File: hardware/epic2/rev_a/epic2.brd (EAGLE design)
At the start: 23.5 x 17 mm, 32 parts, among them J1 PINHD-1X10/0.050, J2 PINHD-1X10/0.050, J3 PINHD-1X10/0.050, U2 FM25LBTDFN-8, U3 CC2538, X1 EPSON-FA-128, X2 FC-12M32.7680KA-A3

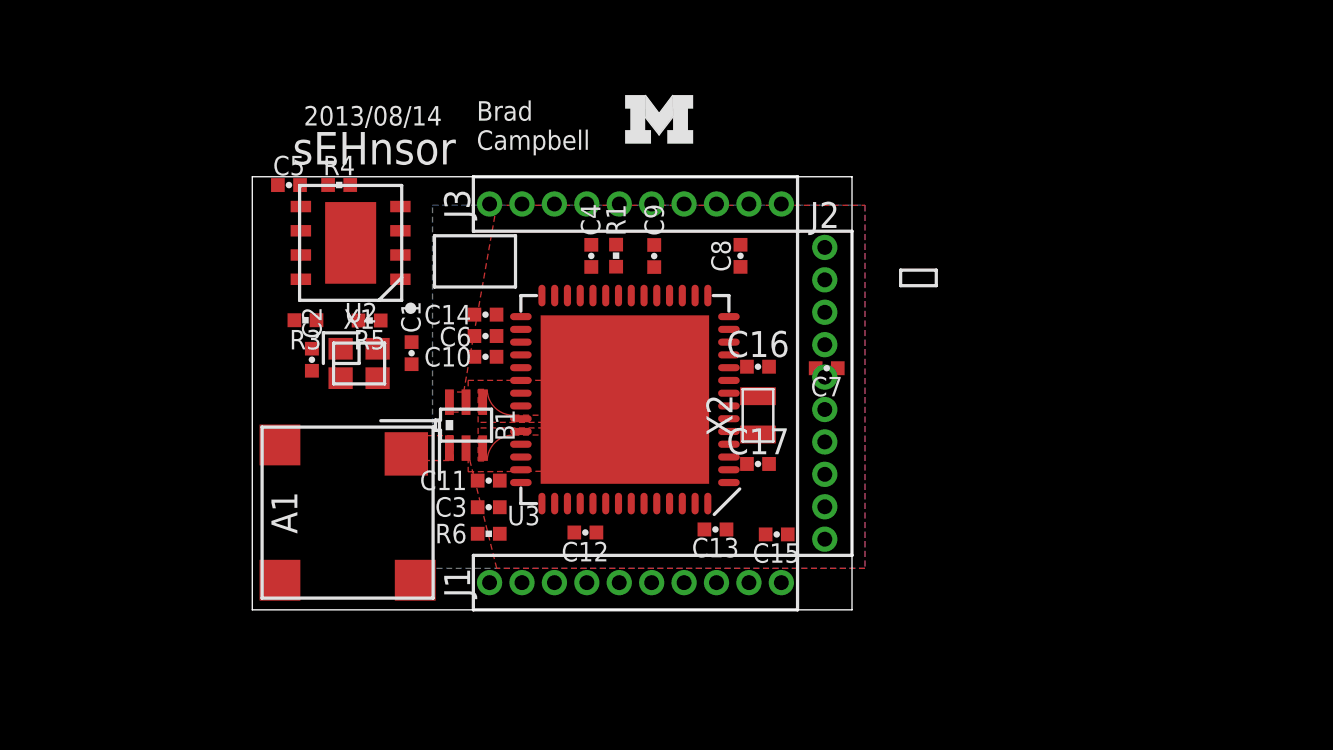
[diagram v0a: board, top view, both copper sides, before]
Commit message: new headers
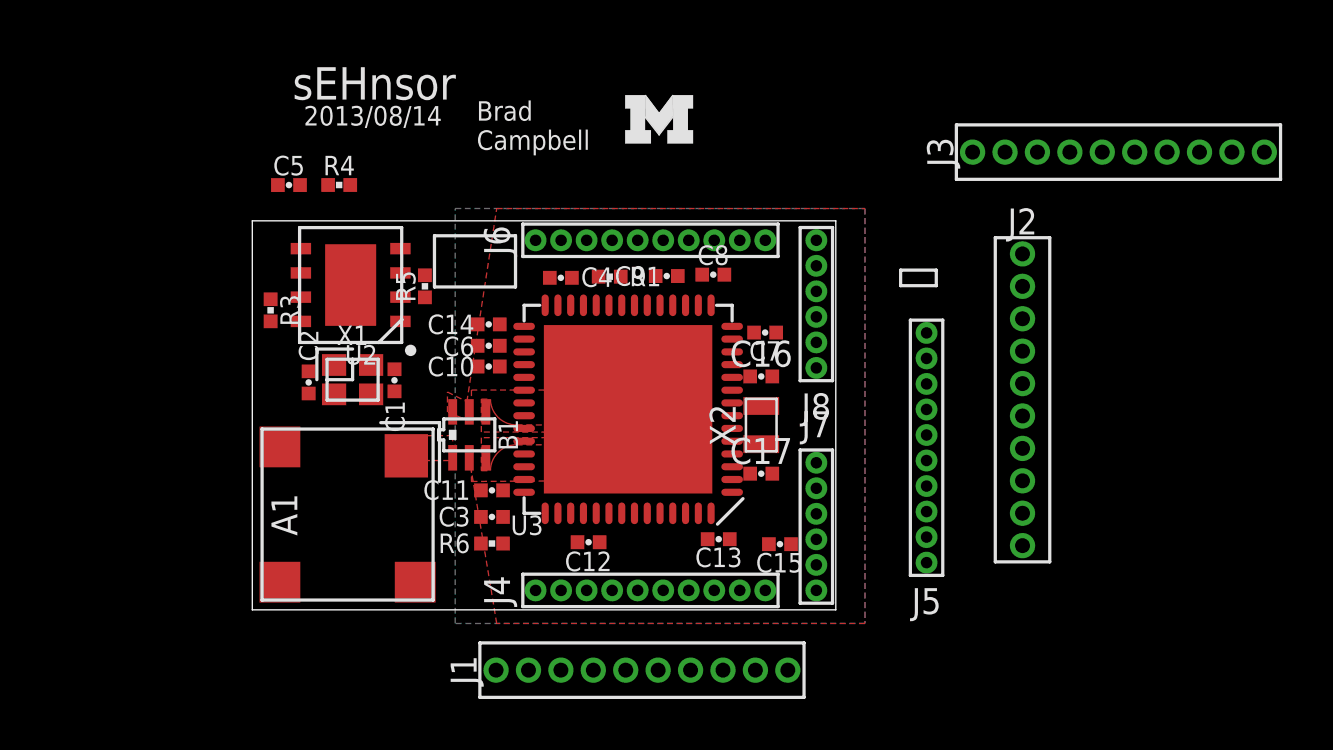
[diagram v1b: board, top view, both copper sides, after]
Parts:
- added J4, J5, J6: PINHD-1X10/1MM, headers:1X10/1MM
- added J7, J8: PINHD-1X06/1MM, headers:1X6/1MM
- moved J3 19.0 mm to (33.9, 17.9)
- moved J2 7.75 mm to (30.2, 8.23)
- moved J1 3.44 mm to (15.3, -2.36)
- moved C7 2.79 mm to (20.1, 10.9)
- moved R5 2.55 mm to (6.76, 12.7), turned to 270 degrees
- moved U2 1.65 mm to (3.85, 12.7)
- moved C4 1.47 mm to (12.1, 13.0), turned to 0 degrees
- moved R3 1.42 mm to (0.72, 11.7), turned to 270 degrees
- moved C8 1.30 mm to (18.1, 13.1), turned to 0 degrees
- moved C1 1.26 mm to (5.57, 8.99), turned to 270 degrees
- moved C9 0.93 mm to (16.2, 13.1), turned to 180 degrees
- moved C2 0.90 mm to (2.21, 8.91)
- moved R1 0.86 mm to (14.0, 13.1), turned to 180 degrees
- moved X1 0.68 mm to (3.93, 9.02)
- moved C10 0.40 mm to (9.26, 9.53)
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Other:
- board size 23.5 x 17 mm -> 22.9 x 15.2 mm

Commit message: dummy routing for epic2
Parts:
- removed J1, J2, J3: PINHD-1X10/0.050, headers:1X10-0.050
- removed J5: PINHD-1X10/1MM, headers:1X10/1MM
- removed R5: 4.7k, passives:0402_RES
- added C18: 10nF, passives:0402_CAP
- added D1: SML-LX0404SIUPGUSB, leds:1MM_SQ_4PAD
- added R2: 1k, passives:0402_RES
- added U1: RV-4162-C7, chips:MICRO-CRYSTAL-C7
- R3, R4: value 4.7k -> 1k
- moved U$1 20.4 mm to (-3.05, 7.98)
- moved R3 19.9 mm to (20.2, 8.13), turned to 180 degrees
- moved R4 19.3 mm to (20.2, 7.24), turned to 180 degrees
- moved C16 11.5 mm to (10.7, 2.29), turned to 270 degrees
- moved X2 9.09 mm to (12.3, 2.29), turned to 0 degrees
- moved C17 6.70 mm to (14.0, 2.29), turned to 270 degrees
- moved C5 5.14 mm to (5.72, 13.8), turned to 270 degrees
- moved C12 3.90 mm to (9.37, 1.80), turned to 180 degrees
- moved R1 3.69 mm to (10.3, 13.0), turned to 270 degrees
- moved C9 2.53 mm to (13.7, 13.1), turned to 0 degrees
- moved C15 1.52 mm to (19.2, 2.83)
- moved U2 1.23 mm to (2.62, 12.8), turned to 270 degrees
- moved C13 1.15 mm to (19.2, 2.06), turned to 0 degrees
- moved C8 1.05 mm to (19.0, 12.7)
- moved C2 1.02 mm to (3.23, 9.04)
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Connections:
- removed net A3: U3.19
- removed net A4: U3.20
- removed net A5: U3.21
- removed net A6: U3.22
- removed net A7: U3.23
- removed net DS2411: U3.5
- removed net MISO: U2.2
- removed net MOSI: U2.5
- removed net SCK: U2.6
- new net !RTC_INT: U1.6, U3.49
- new net ADC3: J6.4, U3.19
- new net ADC4: J6.5, U3.20
- new net ADC5: J6.6, U3.21
- new net ADC6: J6.7, U3.22
- new net ADC7: J6.8, U3.23
- new net B1: J4.10, U3.54
- new net B2: J4.9, U3.53
- new net B3: J4.8, U3.52
- new net B4: J4.7, U3.51
- new net DGND_USB: J7.1, U3.1
- new net DVDD_USB: J7.4, U3.4
- new net I2C_SCL: J8.2, U1.8, U3.8
- new net I2C_SDA: J8.3, U1.1, U3.9
- new net LED_BLUE: R4.2, U3.6
- new net LED_GREEN: R3.2, U3.7
- new net LED_RED: R2.2, U3.5
- new net N$11: D1.4, R3.1
- new net N$12: D1.3, R4.1
- new net N$7: D1.2, R2.1
- new net RTC_CLKOUT: U1.2, U3.50
- new net SPI_MISO: J7.5, U2.2, U3.25
- new net SPI_MOSI: J7.6, U2.5, U3.26
- new net SPI_SCK: J8.1, U2.6, U3.27
- new net UNUSED1: J4.2
- new net UNUSED2: J4.3
- new net USB_N: J7.3, U3.3
- new net USB_P: J7.2, U3.2
- net !FRAM_CS: now also U3.30; no longer R3.1, U3.51
- net !FRAM_HOLD: now also U3.29; no longer R4.1, U3.52
- net !FRAM_WP: now also U3.31; no longer R5.1, U3.50
- net !RESET: now also J6.9
- net BOOTLOADER_CTRL: now also J6.3
- net BOOTLOADER_RX: now also J6.1
- net BOOTLOADER_TX: now also J6.2
- net C0: now also J8.6
- net C1: now also J8.5
- net C2: now also J8.4
- net GND: now also C18.2, J6.10, U1.3
- net TCK: now also J4.5
- net TDO: now also J4.6
- net TMS: now also J4.4
- net VCC: now also C18.1, D1.1, J4.1, U1.5; no longer R3.2, R4.2, R5.2
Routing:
- net RTC_CLKOUT: track 0.00 -> 26.2 mm, vias 0 -> 2
- net !RTC_INT: track 0.00 -> 23.8 mm, vias 0 -> 2
- net VCC: track 0.00 -> 22.0 mm
- net I2C_SDA: track 0.00 -> 22.0 mm, vias 0 -> 1
- net I2C_SCL: track 0.00 -> 20.3 mm, vias 0 -> 1
- net SPI_MISO: track 0.00 -> 14.7 mm, vias 0 -> 2
- net !FRAM_CS: track 0.00 -> 13.3 mm, vias 0 -> 2
- net !FRAM_WP: track 0.00 -> 11.5 mm, vias 0 -> 2
- net SPI_MOSI: track 0.00 -> 11.0 mm, vias 0 -> 2
- net N$10: track 0.00 -> 9.73 mm, vias 0 -> 2
- net SPI_SCK: track 0.00 -> 7.80 mm, vias 0 -> 2
- net !FRAM_HOLD: track 0.00 -> 6.97 mm, vias 0 -> 2
- net N$9: track 0.00 -> 5.44 mm, vias 0 -> 2
- net DGND_USB: track 0.00 -> 5.21 mm
- net B1: track 0.00 -> 4.93 mm
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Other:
- board text added: "BC"
- board text removed: "Brad Campbell"

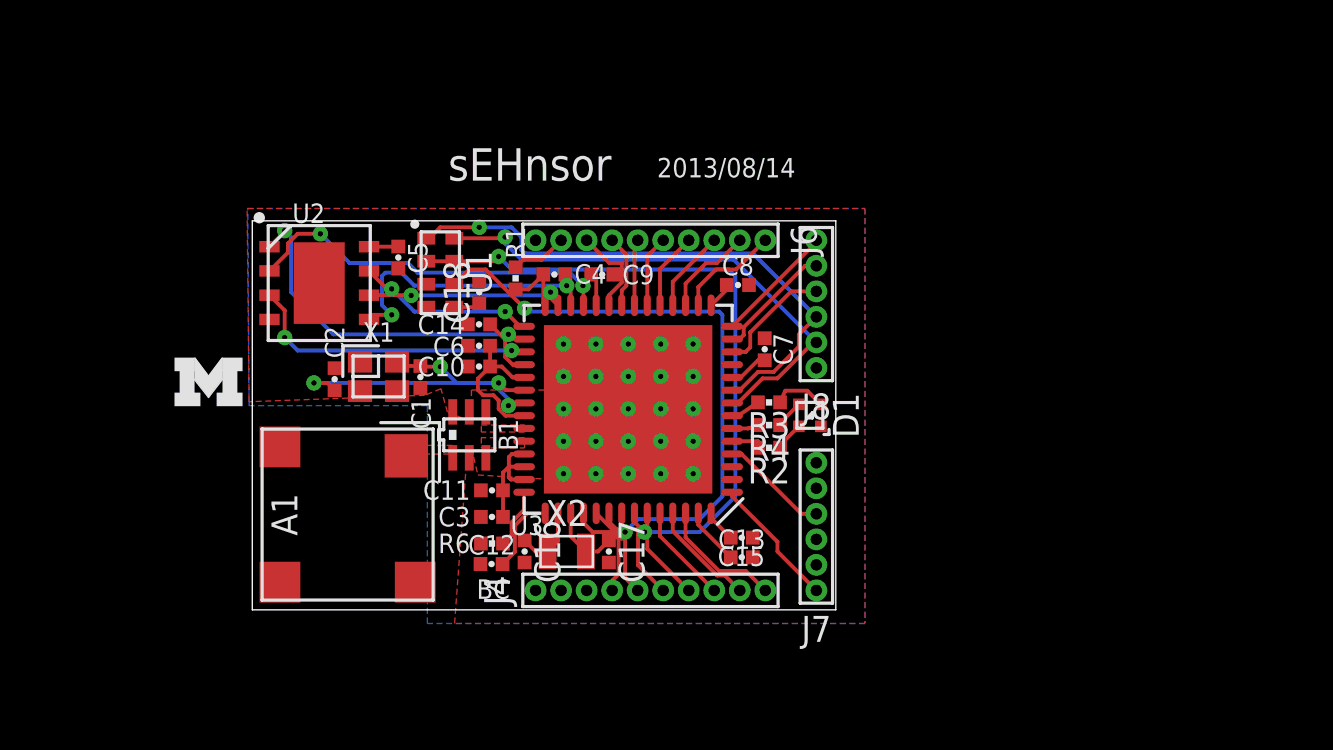
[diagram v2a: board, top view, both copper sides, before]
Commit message: rectangular board close to routed
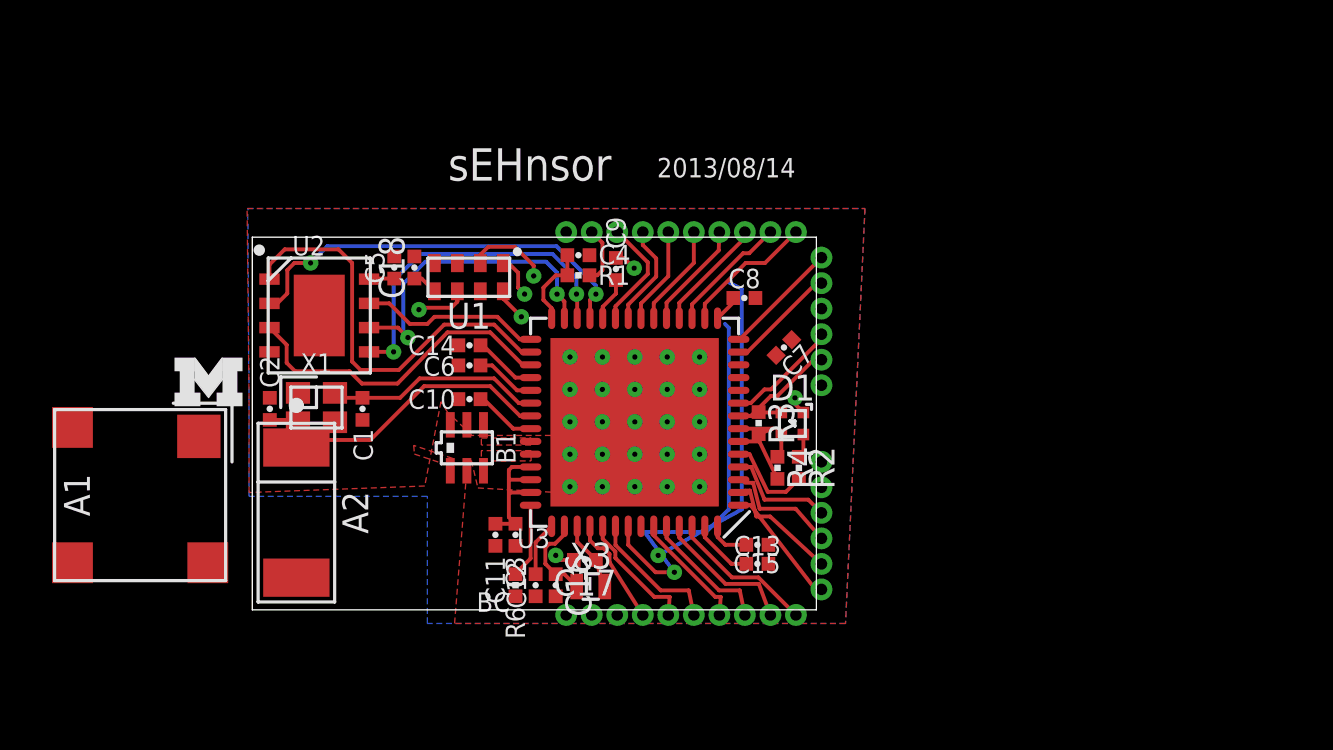
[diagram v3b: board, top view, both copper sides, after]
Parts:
- removed J4, J6: PINHD-1X10/1MM, headers:1X10/1MM
- removed J7, J8: PINHD-1X06/1MM, headers:1X6/1MM
- removed X2: FC-12M32.7680KA-A3, crystals:FC-12M
- added A2: FRACTUS-2.4GHZ-FR05-S1-N-0-102, chips:FRACTUS-ANTENNA-FR05-S1-N-0-102
- added U$2: EPIC2-HEADER, epic2:EPIC2-HEADER
- added X3: ABS05-32.768KHZ-T, crystals:ABS05
- moved A1 8.16 mm to (-4.39, 4.50)
- moved C2 2.79 mm to (0.69, 7.87)
- moved X1 2.72 mm to (2.51, 7.92)
- moved C18 2.72 mm to (6.35, 13.4)
- moved C1 2.59 mm to (4.32, 7.87)
- moved R1 2.46 mm to (12.8, 13.1), turned to 180 degrees
- moved C12 1.92 mm to (11.1, 0.97), turned to 270 degrees
- moved R6 1.88 mm to (10.3, 0.97), turned to 270 degrees
- moved C16 1.80 mm to (11.9, 0.97)
- moved C11 1.75 mm to (9.53, 2.94), turned to 270 degrees
- moved R4 1.71 mm to (20.6, 5.56), turned to 270 degrees
- moved R2 1.41 mm to (21.4, 5.56), turned to 270 degrees
- moved C10 1.33 mm to (8.51, 8.26)
- moved U2 1.27 mm to (2.62, 11.5)
- moved C4 1.21 mm to (12.8, 13.9)
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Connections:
- net !RESET: now also U$2.31; no longer J6.9
- net ADC3: now also U$2.26; no longer J6.4
- net ADC4: now also U$2.27; no longer J6.5
- net ADC5: now also U$2.28; no longer J6.6
- net ADC6: now also U$2.29; no longer J6.7
- net ADC7: now also U$2.30; no longer J6.8
- net B1: now also U$2.10; no longer J4.10
- net B2: now also U$2.9; no longer J4.9
- net B3: now also U$2.8; no longer J4.8
- net B4: now also U$2.7; no longer J4.7
- net BOOTLOADER_CTRL: now also U$2.25; no longer J6.3
- net BOOTLOADER_RX: now also U$2.23; no longer J6.1
- net BOOTLOADER_TX: now also U$2.24; no longer J6.2
- net C0: now also U$2.22; no longer J8.6
- net C1: now also U$2.21; no longer J8.5
- net C2: now also U$2.20; no longer J8.4
- net DGND_USB: now also U$2.11; no longer J7.1
- net DVDD_USB: now also U$2.14; no longer J7.4
- net GND: now also U$2.32; no longer J6.10
- net I2C_SCL: now also U$2.18; no longer J8.2
- net I2C_SDA: now also U$2.19; no longer J8.3
- net N$13: now also X3.B; no longer X2.2
- net N$6: now also X3.A; no longer X2.1
- net SPI_MISO: now also U$2.15; no longer J7.5
- net SPI_MOSI: now also U$2.16; no longer J7.6
- net SPI_SCK: now also U$2.17; no longer J8.1
- net TCK: now also U$2.5; no longer J4.5
- net TDO: now also U$2.6; no longer J4.6
- net TMS: now also U$2.4; no longer J4.4
- net UNUSED1: now also U$2.2; no longer J4.2
- net UNUSED2: now also U$2.3; no longer J4.3
- net USB_N: now also U$2.13; no longer J7.3
- net USB_P: now also U$2.12; no longer J7.2
- net VCC: now also U$2.1; no longer J4.1
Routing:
- net I2C_SDA: track 22.0 -> 6.15 mm
- net I2C_SCL: track 20.3 -> 5.45 mm
- net RTC_CLKOUT: track 26.2 -> 16.5 mm
- net !RTC_INT: track 23.8 -> 18.4 mm
- net SPI_SCK: track 7.80 -> 12.7 mm
- net C2: track 4.62 -> 0.00 mm
- net USB_P: track 0.00 -> 4.51 mm
- net USB_N: track 0.00 -> 4.32 mm
- net !FRAM_CS: track 13.3 -> 16.4 mm, vias 2 -> 0
- net N$9: track 5.44 -> 8.50 mm, vias 2 -> 0
- net SPI_MOSI: track 11.0 -> 13.3 mm
- net LED_RED: track 1.27 -> 3.49 mm
- net N$10: track 9.73 -> 11.9 mm, vias 2 -> 0
- net GND: track 0.00 -> 1.66 mm, vias 9 -> 27
- net SPI_MISO: track 14.7 -> 16.3 mm
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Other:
- board size 22.9 x 15.2 mm -> 22.1 x 14.6 mm

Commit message: workin on epic2
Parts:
- removed U$2: EPIC2-HEADER, epic2:EPIC2-HEADER
- added J1: EPIC2-HEADER2, epic2:EPIC2-HEADER2
- moved R2 26.5 mm to (-2.46, 17.0)
- moved R4 25.1 mm to (-1.78, 17.0)
- moved R3 23.0 mm to (-0.99, 17.0)
- moved D1 22.4 mm to (0.95, 17.0), turned to 90 degrees
- moved U2 4.83 mm to (5.42, 15.5)
- moved X3 4.29 mm to (8.97, 0.89)
- moved C12 4.17 mm to (6.93, 1.09)
- moved C16 4.17 mm to (7.72, 1.09)
- moved R6 4.17 mm to (6.15, 1.09)
- moved U1 4.12 mm to (11.8, 15.4)
- moved C18 4.09 mm to (9.47, 16.1)
- moved C1 4.09 mm to (3.40, 11.9)
- moved C8 4.09 mm to (15.2, 12.7), turned to 90 degrees
- moved X1 4.01 mm to (1.73, 11.9)
- moved C5 3.72 mm to (8.18, 16.1)
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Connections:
- removed net B1: U$2.10, U3.54
- removed net B2: U$2.9, U3.53
- removed net UNUSED2: U$2.3
- new net B5: J1.7, U3.50
- new net B6: J1.6, U3.49
- net !RESET: now also J1.31; no longer U$2.31
- net !RTC_INT: now also U3.54; no longer U3.49
- net ADC3: now also J1.26; no longer U$2.26
- net ADC4: now also J1.27; no longer U$2.27
- net ADC5: now also J1.28; no longer U$2.28
- net ADC6: now also J1.29; no longer U$2.29
- net ADC7: now also J1.30; no longer U$2.30
- net B3: now also J1.9; no longer U$2.8
- net B4: now also J1.8; no longer U$2.7
- net BOOTLOADER_CTRL: now also J1.25; no longer U$2.25
- net BOOTLOADER_RX: now also J1.23; no longer U$2.23
- net BOOTLOADER_TX: now also J1.24; no longer U$2.24
- net C0: now also J1.22; no longer U$2.22
- net C1: now also J1.21; no longer U$2.21
- net C2: now also J1.20; no longer U$2.20
- net C3: now also J1.19
- net DGND_USB: now also J1.10; no longer U$2.11
- net DVDD_USB: now also J1.13; no longer U$2.14
- net GND: now also J1.32; no longer U$2.32
- net I2C_SCL: now also J1.17; no longer U$2.18
- net I2C_SDA: now also J1.18; no longer U$2.19
- net LED_BLUE: no longer U3.6
- net LED_GREEN: no longer U3.7
- net LED_RED: no longer U3.5
- net RTC_CLKOUT: now also U3.53; no longer U3.50
- net SPI_MISO: now also J1.14, U3.5; no longer U$2.15
- net SPI_MOSI: now also J1.15, U3.6; no longer U$2.16
- net SPI_SCK: now also J1.16, U3.7; no longer U$2.17
- net TCK: now also J1.4; no longer U$2.5
- net TDO: now also J1.5; no longer U$2.6
- net TMS: now also J1.3; no longer U$2.4
- net UNUSED1: now also J1.2; no longer U$2.2
- net USB_N: now also J1.12; no longer U$2.13
- net USB_P: now also J1.11; no longer U$2.12
- net VCC: now also J1.1; no longer U$2.1
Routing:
- net !FRAM_WP: track 12.9 -> 3.86 mm
- net !RTC_INT: track 18.4 -> 9.61 mm, vias 2 -> 1
- net N$10: track 11.9 -> 4.70 mm
- net B1: track 5.76 -> 0.00 mm
- net B2: track 5.61 -> 0.00 mm
- net BOOTLOADER_RX: track 5.30 -> 0.00 mm
- net !FRAM_CS: track 16.4 -> 11.2 mm
- net BOOTLOADER_TX: track 4.79 -> 0.00 mm
- net C0: track 4.57 -> 0.04 mm
- net VCC: track 20.5 -> 16.0 mm, vias 1 -> 0
- net BOOTLOADER_CTRL: track 4.45 -> 0.00 mm
- net ADC3: track 4.22 -> 0.00 mm
- net ADC4: track 4.03 -> 0.00 mm
- net C1: track 4.36 -> 0.34 mm
- net B5: track 0.00 -> 3.92 mm
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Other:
- board size 22.1 x 14.6 mm -> 18 x 18 mm
- board text removed: "2013/08/14"
- board text removed: "sEHnsor"

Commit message: getting closer with epic2
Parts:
- removed A1: FRACTUS-2.4GHZ-FR05-S1-N-0-001, chips:FRACTUS-ANTENNA-FR05-S1-N-0-001
- removed C7: 0.1uF, passives:0402_CAP
- added C20: 0.1uF, rcl:C0201
- moved R2 5.21 mm to (2.41, 15.2)
- moved R4 3.86 mm to (1.63, 15.2)
- moved C4 3.59 mm to (6.38, 12.1), turned to 90 degrees
- moved R1 2.59 mm to (7.19, 12.1), turned to 270 degrees
- moved R3 2.55 mm to (0.84, 15.2)
- moved C9 1.70 mm to (9.57, 13.4)
- moved C18 1.47 mm to (10.9, 16.3), turned to 270 degrees
- moved C8 1.43 mm to (16.4, 11.8)
- moved C1 0.83 mm to (3.02, 11.1), turned to 90 degrees
- moved C5 0.67 mm to (8.71, 16.5), turned to 270 degrees
- moved U1 0.60 mm to (12.3, 15.0), turned to 90 degrees
- moved X1 0.54 mm to (1.27, 12.1), turned to 270 degrees
- moved D1 0.40 mm to (1.22, 16.7)
- moved U2 0.30 mm to (5.72, 15.5)
- moved C2 0.28 mm to (1.45, 10.4), turned to 180 degrees
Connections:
- new net UNUSED2: J1.22
- net !FRAM_CS: now also U3.26; no longer U3.30
- net !FRAM_HOLD: now also U3.25; no longer U3.29
- net !FRAM_WP: now also U3.27; no longer U3.31
- net ANTENNA: now also A2.1; no longer A1.1
- net C0: now also J1.21; no longer J1.22
- net C1: now also J1.20; no longer J1.21
- net C2: now also J1.19; no longer J1.20
- net C3: no longer J1.19
- net GND: now also C20.2; no longer C7.2
- net I2C_SCL: now also U3.9; no longer U3.8
- net I2C_SDA: now also U3.8; no longer U3.9
- net LED_BLUE: now also U3.30
- net LED_GREEN: now also U3.31
- net LED_RED: now also U3.29
- net SPI_MISO: no longer U3.25
- net SPI_MOSI: no longer U3.26
- net SPI_SCK: no longer U3.27
- net VCC: now also C20.1; no longer C7.1
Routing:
- net VCC: track 16.0 -> 29.6 mm, vias 0 -> 8
- net SPI_MISO: track 13.7 -> 26.0 mm, vias 2 -> 1
- net ADC5: track 0.00 -> 10.8 mm
- net ADC4: track 0.00 -> 10.1 mm
- net !RTC_INT: track 9.61 -> 19.5 mm, vias 1 -> 2
- net ADC3: track 0.00 -> 9.85 mm
- net LED_GREEN: track 0.00 -> 9.49 mm
- net BOOTLOADER_CTRL: track 0.00 -> 9.16 mm
- net BOOTLOADER_TX: track 0.00 -> 8.79 mm
- net LED_BLUE: track 0.00 -> 8.58 mm
- net GND: track 3.87 -> 11.7 mm, vias 28 -> 33
- net LED_RED: track 0.00 -> 7.55 mm
- net SPI_MOSI: track 11.9 -> 19.4 mm
- net SPI_SCK: track 11.3 -> 18.5 mm
- net BOOTLOADER_RX: track 0.00 -> 7.01 mm
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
